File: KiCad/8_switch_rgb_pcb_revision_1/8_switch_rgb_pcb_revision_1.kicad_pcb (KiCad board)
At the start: 2 copper layers, 100 x 100 mm, 106 parts, among them SW0 SW0, SW1 SW1, SW2 SW2, SW3 SW3, SW4 SW4, SW5 SW5, SW6 SW6, SW7 SW7, U2 74HC165, Y1 16MHz

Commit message: Added gerbers, will look at ground plane
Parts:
- added ?: , , F.Cu at (203.9, 93.1)
- added ?: , , F.Cu at (203.0, 77.2)
- added ?: , , F.Cu at (203.9, 92.0)
- added ?: , , F.Cu at (203.0, 74.6)
- moved R40 5.09 mm to (125.1, 113.8), turned to -90 degrees
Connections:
- R22 pad 1: Net-(MCU_1-PB5) -> Net-(U2-CP)
- R40 pad 2: Net-(MCU_1-PB5) -> Net-(U2-CP)
- U2 pad 2: Net-(MCU_1-PB5) -> Net-(U2-CP)
- U_Drain1 pad 15: Net-(MCU_1-PB5) -> Net-(U2-CP)
- U_Trans1 pad 11: Net-(MCU_1-PB5) -> Net-(U2-CP)
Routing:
- net Net-(U2-CP): track 0.00 -> 66.2 mm
- net Net-(MCU_1-PB5): track 68.8 -> 2.55 mm
- net Net-(MCU_1-PB4): track 147.6 -> 127.4 mm
- net Net-(SW0-B): track 98.9 -> 90.8 mm
- net Net-(C_TERM_GND0-Pad2): track 6.65 -> 9.65 mm
- net GND: track 480.8 -> 478.8 mm
- net Net-(D0-A): track 174.1 -> 172.2 mm
- net Net-(U_Drain1-DRAIN7): track 120.4 -> 121.7 mm, vias 4 -> 2
- net +5V: track 575.3 -> 574.4 mm
- net Net-(MCU_1-PC5): track 112.8 -> 113.7 mm
- net Net-(U_Drain1-DRAIN6): track 124.9 -> 124.8 mm, vias 5 -> 3
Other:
- board text added: "8_switch_rgb_rev1 MARCH 2024 David Per Carlsson"

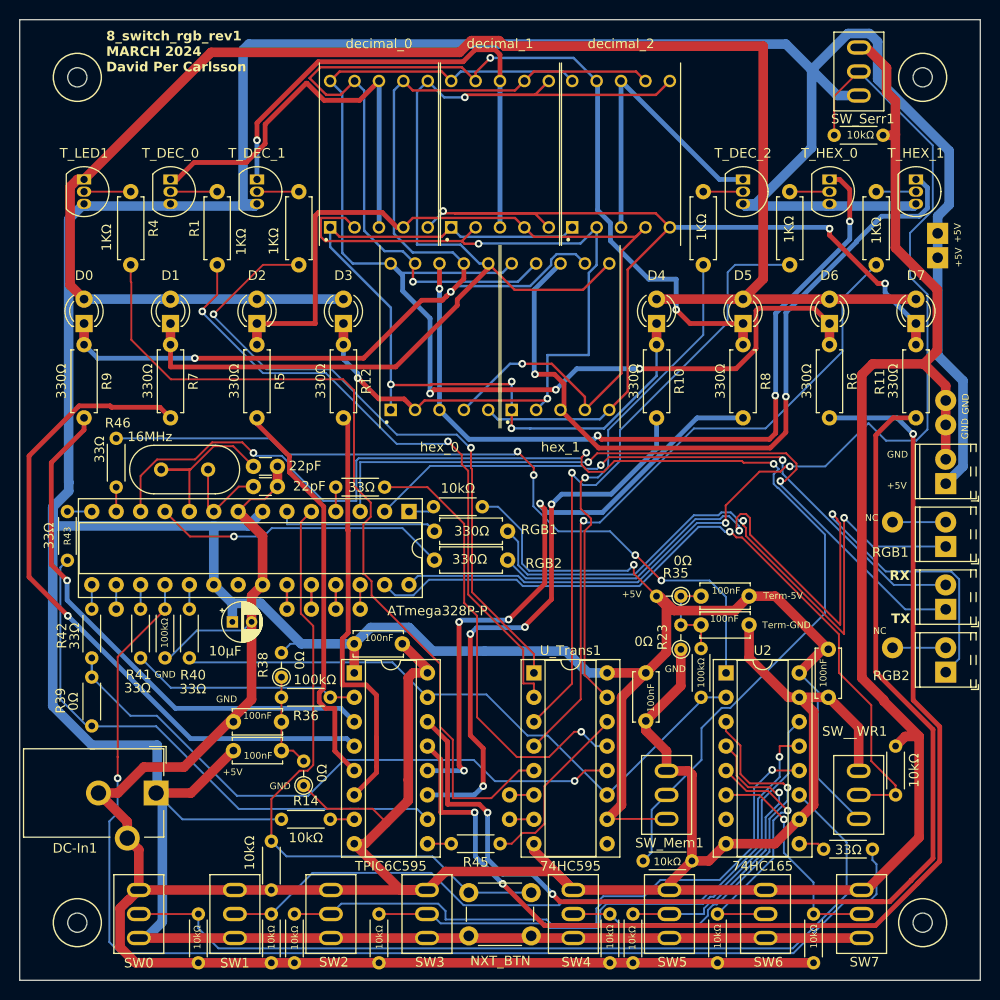
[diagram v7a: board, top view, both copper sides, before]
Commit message: Added the zip from pcbway. Will order both with ground fill and without
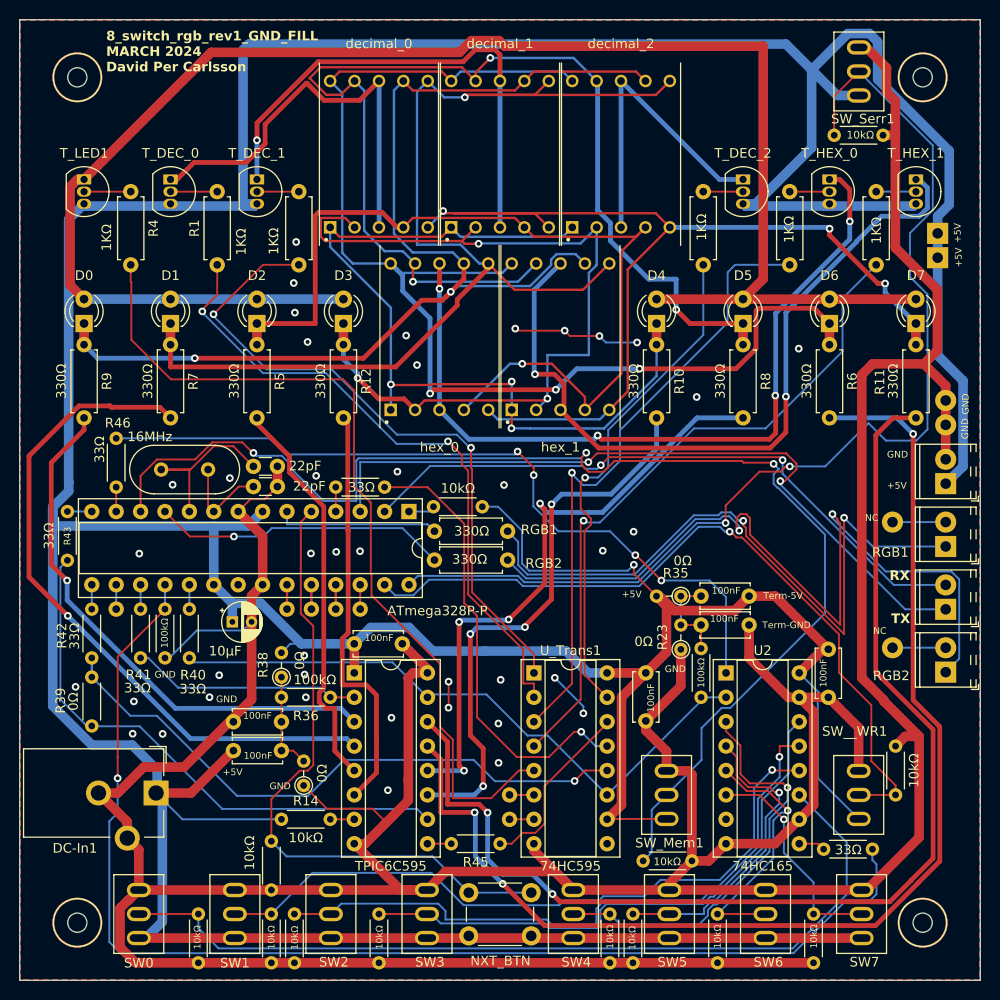
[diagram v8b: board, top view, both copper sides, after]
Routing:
- net GND: track 478.8 -> 499.8 mm, vias 0 -> 41
- net +5V: track 574.4 -> 572.8 mm
- net Net-(U_Trans1-QF): track 90.3 -> 89.6 mm
- added copper zone on B.Cu, net GND
- added copper zone on F.Cu, net GND
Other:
- board text added: "8_switch_rgb_rev1_GND_FILL MARCH 2024 David Per Carlsson"
- board text removed: "8_switch_rgb_rev1 MARCH 2024 David Per Carlsson"
